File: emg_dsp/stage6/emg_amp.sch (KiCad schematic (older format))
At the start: 17 parts, among them U183 MAX4208

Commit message: finalizing schematic - next to do: check footprints.
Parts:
- U183: footprint MSOP-8 -> uMAX-8
- U?: footprint (none) -> TSSOP-14
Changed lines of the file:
@@
-EESchema Schematic File Version 2  date Fri 24 Sep 2010 11:59:53 PM EDT
-LIBS:power
-LIBS:device
-LIBS:emg_sym
-LIBS:linear
-LIBS:stage6-cache
+EESchema Schematic File Version 2  date Mon 27 Sep 2010 12:50:24 AM EDT
+LIBS:power,device,emg_sym,/home/tlh24/svn/myopen/emg_dsp/lib/linear
 EELAYER 24  0
 EELAYER END
 $Descr A4 11700 8267
-Sheet 10 13
+Sheet 3 13
 Title "Stage 4 / Copyright 2010 Timothy L Hanson "
 Date "25 sep 2010"
@@
 U 1 1 4C9D733B
 P 1950 4000
+AR Path="/4C9BA165/4C9D5FEB/4C9D733B" Ref="TP?"  Part="1"
+AR Path="/4C9BA165/4C9D6BB6/4C9D733B" Ref="TP?"  Part="1"
 F 0 "TP?" H 1950 4000 60  0000 C CNN
 F 1 "TP" H 1800 3950 60  0000 C CNN
@@
 U 1 1 4C9D732E
 P 1950 3200
+AR Path="/4C9BA165/4C9D5FEB/4C9D732E" Ref="TP?"  Part="1"
+AR Path="/4C9BA165/4C9D6BB6/4C9D732E" Ref="TP?"  Part="1"
 F 0 "TP?" H 1950 3200 60  0000 C CNN
 F 1 "TP" H 1800 3150 60  0000 C CNN
@@
 $Comp
 L OPA4348 U?
-U 1 1 4C9D6A40
+U 2 1 4C9D6A40
 P 6100 3550
 AR Path="/4C9BA165/4C9D5FEB/4C9D6A40" Ref="U?"  Part="1"
@@
 F 0 "U?" H 5900 3550 60  0000 C CNN
 F 1 "OPA4348" H 5900 4300 60  0000 C CNN
-	1    6100 3550
+F 2 "TSSOP-14" H 5840 3490 60  0000 C CNN
+	2    6100 3550
 	1    0    0    -1
 $EndComp
@@
 F 0 "U177" H 3200 3350 60  0000 C CNN
 F 1 "MAX4208" H 3250 3850 60  0000 C CNN
-F 2 "MSOP-8" H 3140 3290 60  0000 C CNN
+F 2 "uMAX-8" H 3140 3290 60  0000 C CNN
 	1    3200 3600
 	1    0    0    -1

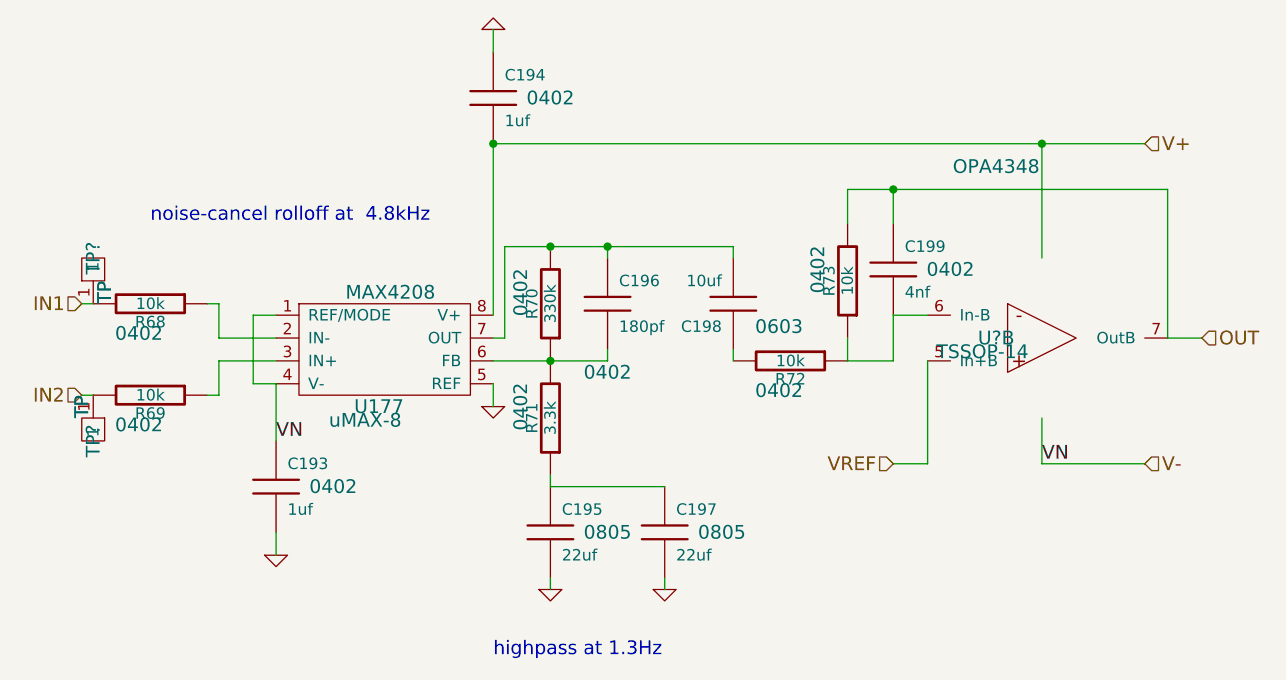
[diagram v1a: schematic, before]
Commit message: need to make the footprint for the ethernet MAC, then ready to layout ...
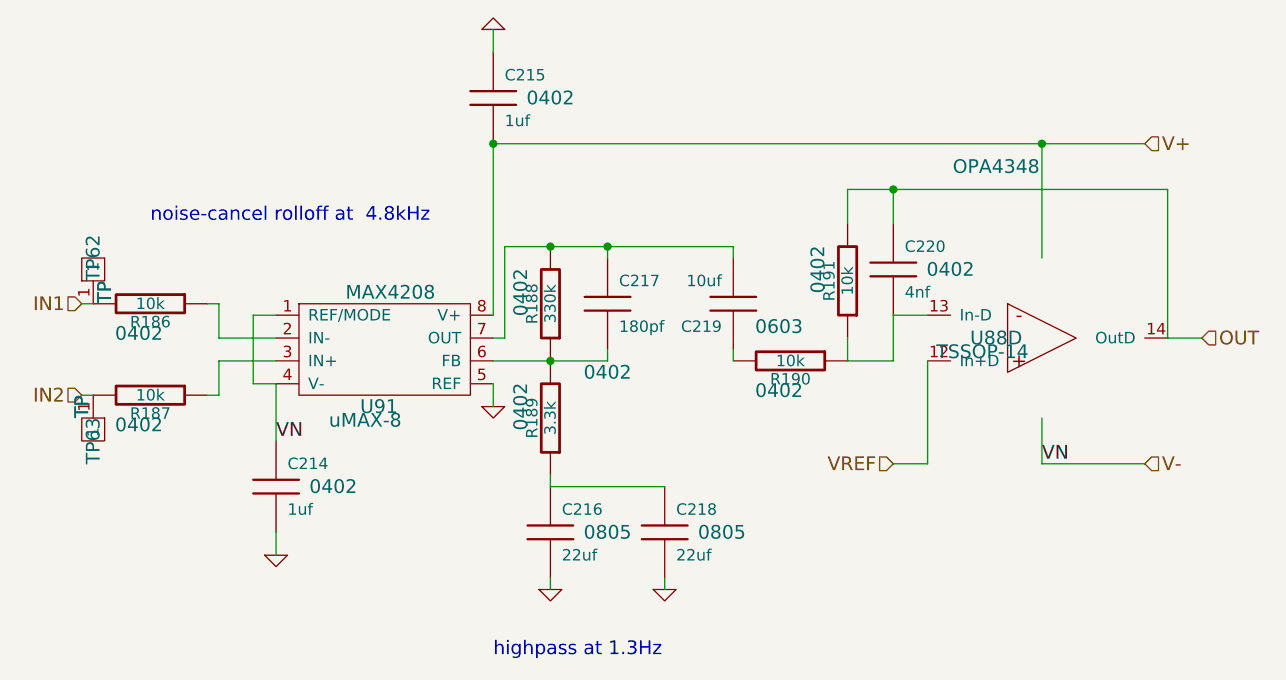
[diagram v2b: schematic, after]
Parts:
- gave numbers to parts that had none: 3
- renumbered C211 to C172, C212 to C173, C213 to C174, C214 to C175, C215 to C176, C216 to C177, C217 to C178, R82 to R150, R83 to R151, R84 to R152, R85 to R153, R86 to R154, R87 to R155, U183 to U84

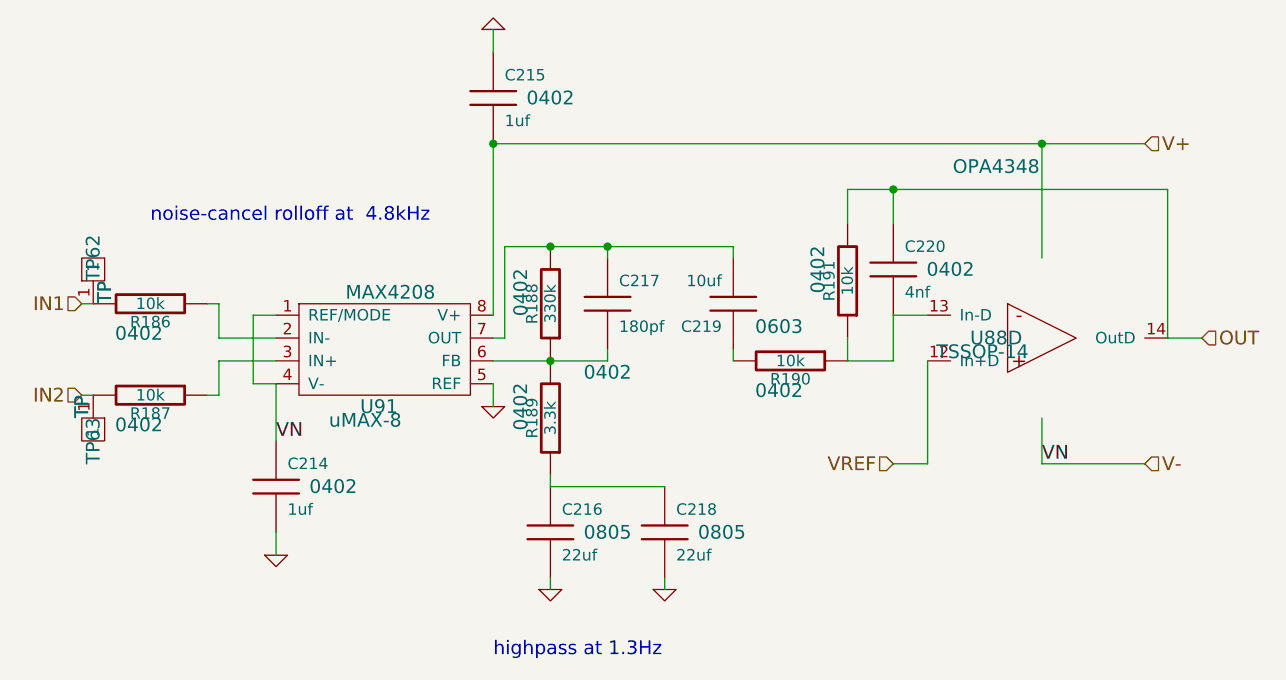
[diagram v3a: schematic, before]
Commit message: part placement for stage 6 - going to be a moderately large board..
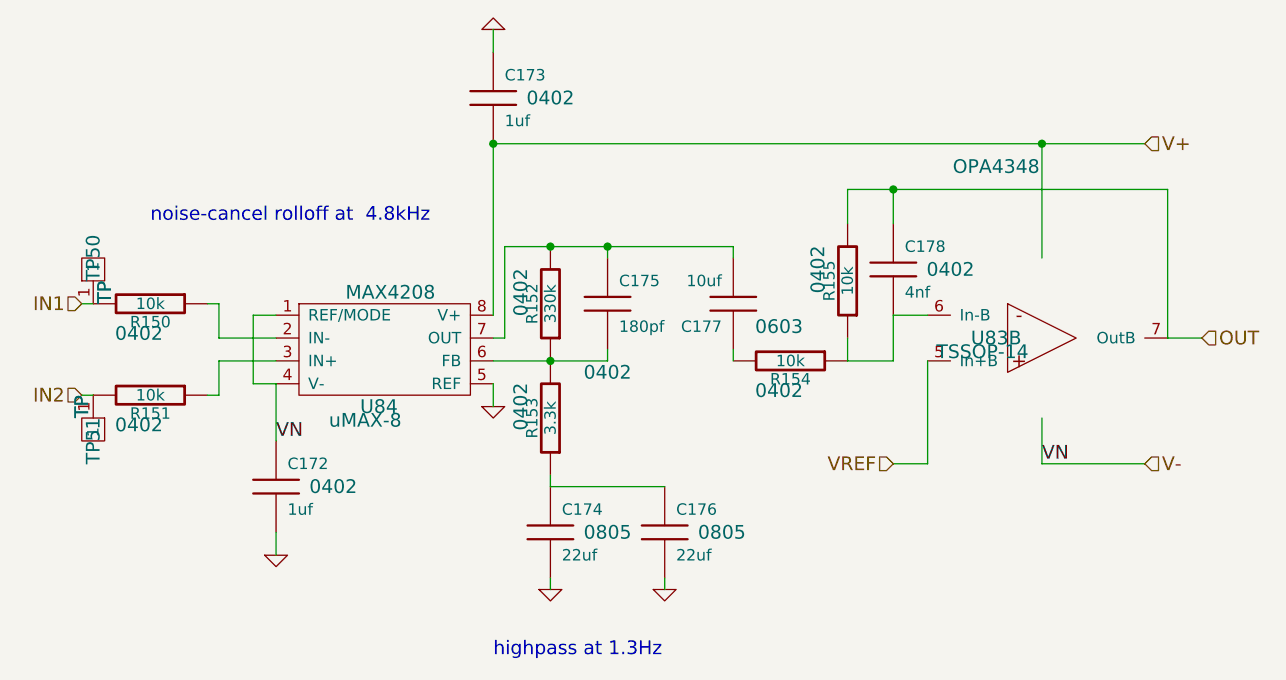
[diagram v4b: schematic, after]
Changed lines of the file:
@@
-EESchema Schematic File Version 2  date Mon 27 Sep 2010 01:11:23 PM EDT
+EESchema Schematic File Version 2  date Mon 27 Sep 2010 05:14:30 PM EDT
 LIBS:power
 LIBS:device
@@
 EELAYER END
 $Descr A4 11700 8267
-Sheet 4 13
+Sheet 10 13
 Title "Stage 4 / Copyright 2010 Timothy L Hanson "
 Date "27 sep 2010"
@@
 AR Path="/4C9BA165/4C9D6BC0/4C9D733B" Ref="TP53"  Part="1"
 AR Path="/4C9BA165/4C9D5FEB/4C9D733B" Ref="TP49"  Part="1"
-F 0 "TP63" H 1950 4000 60  0000 C CNN
+F 0 "TP51" H 1950 4000 60  0000 C CNN
 F 1 "TP" H 1800 3950 60  0000 C CNN
 F 2 "TP" H 1800 3950 60  0000 C CNN
@@
 AR Path="/4C9BA165/4C9D6BC0/4C9D732E" Ref="TP52"  Part="1"
 AR Path="/4C9BA165/4C9D5FEB/4C9D732E" Ref="TP48"  Part="1"
-F 0 "TP62" H 1950 3200 60  0000 C CNN
+F 0 "TP50" H 1950 3200 60  0000 C CNN
 F 1 "TP" H 1800 3150 60  0000 C CNN
 F 2 "TP" H 1800 3150 60  0000 C CNN
@@
 $Comp
 L OPA4348 U83
-U 4 1 4C9D6A40
+U 2 1 4C9D6A40
 P 6100 3550
 AR Path="/4C9BA165/4C9D6BB6/4C9D6A40" Ref="U83"  Part="2"
@@
 AR Path="/4C9BA165/4C9D6BC0/4C9D6A40" Ref="U83"  Part="3"
 AR Path="/4C9BA165/4C9D5FEB/4C9D6A40" Ref="U83"  Part="1"
-F 0 "U88" H 5900 3550 60  0000 C CNN
+F 0 "U83" H 5900 3550 60  0000 C CNN
 F 1 "OPA4348" H 5900 4300 60  0000 C CNN
 F 2 "TSSOP-14" H 5840 3490 60  0000 C CNN
-	4    6100 3550
+	2    6100 3550
 	1    0    0    -1
 $EndComp
@@
 AR Path="/4C9BA165/4C9D6BC0/4B607777" Ref="C184"  Part="1"
 AR Path="/4C9BA165/4C9D5FEB/4B607777" Ref="C170"  Part="1"
-F 0 "C219" H 4800 3500 50  0000 L CNN
+F 0 "C177" H 4800 3500 50  0000 L CNN
 F 1 "10uf" H 4800 3300 50  0000 L CNN
 F 2 "0603" H 4550 3500 60  0000 C CNN
@@
 AR Path="/4C9BA165/4C9D6BC0/4B5E8316" Ref="C180"  Part="1"
 AR Path="/4C9BA165/4C9D5FEB/4B5E8316" Ref="C166"  Part="1"
-F 0 "C215" H 3750 2600 50  0000 L CNN
+F 0 "C173" H 3750 2600 50  0000 L CNN
 F 1 "1uf" H 3750 2400 50  0000 L CNN
 F 2 "0402" H 3950 2500 60  0000 C CNN
@@
 AR Path="/4C9BA165/4C9D6BC0/4B5E82D0" Ref="C179"  Part="1"
 AR Path="/4C9BA165/4C9D5FEB/4B5E82D0" Ref="C165"  Part="1"
-F 0 "C214" H 2800 4300 50  0000 L CNN
+F 0 "C172" H 2800 4300 50  0000 L CNN
 F 1 "1uf" H 2800 4100 50  0000 L CNN
 F 2 "0402" H 3000 4200 60  0000 C CNN
@@
 AR Path="/4C9BA165/4C9D6BC0/4B5E2EEF" Ref="C185"  Part="1"
 AR Path="/4C9BA165/4C9D5FEB/4B5E2EEF" Ref="C171"  Part="1"
-F 0 "C220" H 5500 3350 50  0000 L CNN
+F 0 "C178" H 5500 3350 50  0000 L CNN
 F 1 "4nf" H 5500 3150 50  0000 L CNN
 F 2 "0402" H 5700 3250 60  0000 C CNN
@@
 AR Path="/4C9BA165/4C9D6BC0/4B5E2EB2" Ref="R161"  Part="1"
 AR Path="/4C9BA165/4C9D5FEB/4B5E2EB2" Ref="R149"  Part="1"
-F 0 "R191" V 5330 3300 50  0000 C CNN
+F 0 "R155" V 5330 3300 50  0000 C CNN
 F 1 "10k" V 5250 3300 50  0000 C CNN
 F 2 "0402" V 5380 3250 60  0000 C CNN
@@
 AR Path="/4C9BA165/4C9D6BC0/4B5E2EA6" Ref="R160"  Part="1"
 AR Path="/4C9BA165/4C9D5FEB/4B5E2EA6" Ref="R148"  Part="1"
-F 0 "R190" V 5080 3650 50  0000 C CNN
+F 0 "R154" V 5080 3650 50  0000 C CNN
 F 1 "10k" V 5000 3650 50  0000 C CNN
 F 2 "0402" V 5130 3600 60  0000 C CNN
@@
 AR Path="/4C9BA165/4C9D6BC0/4B5E2BEE" Ref="C183"  Part="1"
 AR Path="/4C9BA165/4C9D5FEB/4B5E2BEE" Ref="C169"  Part="1"
-F 0 "C218" H 4500 4500 50  0000 L CNN
+F 0 "C176" H 4500 4500 50  0000 L CNN
 F 1 "22uf" H 4500 4300 50  0000 L CNN
 F 2 "0805" H 4700 4400 60  0000 C CNN
@@
 AR Path="/4C9BA165/4C9D6BC0/4B5E2631" Ref="C182"  Part="1"
 AR Path="/4C9BA165/4C9D5FEB/4B5E2631" Ref="C168"  Part="1"
-F 0 "C217" H 4250 3500 50  0000 L CNN
+F 0 "C175" H 4250 3500 50  0000 L CNN
 F 1 "180pf" H 4250 3300 50  0000 L CNN
 F 2 "0402" H 4200 3100 60  0000 C CNN
@@
 AR Path="/4C9BA165/4C9D6BC0/4B5E2425" Ref="C181"  Part="1"
 AR Path="/4C9BA165/4C9D5FEB/4B5E2425" Ref="C167"  Part="1"
-F 0 "C216" H 4000 4500 50  0000 L CNN
+F 0 "C174" H 4000 4500 50  0000 L CNN
 F 1 "22uf" H 4000 4300 50  0000 L CNN
 F 2 "0805" H 4200 4400 60  0000 C CNN
@@
 AR Path="/4C9BA165/4C9D6BC0/4B5E23F1" Ref="R158"  Part="1"
 AR Path="/4C9BA165/4C9D5FEB/4B5E23F1" Ref="R146"  Part="1"
-F 0 "R188" V 4030 3400 50  0000 C CNN
+F 0 "R152" V 4030 3400 50  0000 C CNN
 F 1 "330k" V 3950 3400 50  0000 C CNN
 F 2 "0402" V 4080 3350 60  0000 C CNN
@@
 AR Path="/4C9BA165/4C9D6BC0/4B5E23EA" Ref="R159"  Part="1"
 AR Path="/4C9BA165/4C9D5FEB/4B5E23EA" Ref="R147"  Part="1"
-F 0 "R189" V 4030 3900 50  0000 C CNN
+F 0 "R153" V 4030 3900 50  0000 C CNN
 F 1 "3.3k" V 3950 3900 50  0000 C CNN
 F 2 "0402" V 4080 3850 60  0000 C CNN
@@
 AR Path="/4C9BA165/4C9D6BC0/4B5E2389" Ref="R157"  Part="1"
 AR Path="/4C9BA165/4C9D5FEB/4B5E2389" Ref="R145"  Part="1"
-F 0 "R187" V 2280 3800 50  0000 C CNN
+F 0 "R151" V 2280 3800 50  0000 C CNN
 F 1 "10k" V 2200 3800 50  0000 C CNN
 F 2 "0402" V 2330 3750 60  0000 C CNN
@@
 AR Path="/4C9BA165/4C9D6BC0/4B5E236D" Ref="R156"  Part="1"
 AR Path="/4C9BA165/4C9D5FEB/4B5E236D" Ref="R144"  Part="1"
-F 0 "R186" V 2280 3400 50  0000 C CNN
+F 0 "R150" V 2280 3400 50  0000 C CNN
 F 1 "10k" V 2200 3400 50  0000 C CNN
 F 2 "0402" V 2330 3350 60  0000 C CNN
@@
 AR Path="/4C9BA165/4C9D6BC0/4B5E2341" Ref="U85"  Part="1"
 AR Path="/4C9BA165/4C9D5FEB/4B5E2341" Ref="U82"  Part="1"
-F 0 "U91" H 3200 3350 60  0000 C CNN
+F 0 "U84" H 3200 3350 60  0000 C CNN
 F 1 "MAX4208" H 3250 3850 60  0000 C CNN
 F 2 "uMAX-8" H 3140 3290 60  0000 C CNN
